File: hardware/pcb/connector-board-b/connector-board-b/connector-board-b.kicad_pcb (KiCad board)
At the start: 2 copper layers, 21.3 x 50.5 mm, 4 parts, among them J1 DE9_Pins, J3 Conn_01x02, J4 Conn_01x02, J5 8-215570-0

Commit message: Updated Connectorboard B to rev. 1.1
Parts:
- removed J3: Conn_01x02, TerminalBlock:TerminalBlock_MaiXu_MX126-5.0-02P_1x02_P5.00mm
- removed J4: Conn_01x02, Connector_JST:JST_EH_B2B-EH-A_1x02_P2.50mm_Vertical
- added C1: 10u 50V, Capacitor_SMD:C_1210_3225Metric, F.Cu at (159.1, 49.8)
- added C10: 100n, Capacitor_SMD:C_0805_2012Metric, F.Cu at (148.4, 51.1)
- added C11: 10u, Capacitor_SMD:C_1206_3216Metric, F.Cu at (145.3, 46.9)
- added C12: 100n, Capacitor_SMD:C_0805_2012Metric, F.Cu at (150.9, 64.3)
- added C13: 1n DNP, Capacitor_SMD:C_0805_2012Metric, F.Cu at (142.3, 79.1)
- added C14: 1u, Capacitor_SMD:C_0805_2012Metric, F.Cu at (147.1, 56.2)
- added C15: 1u, Capacitor_SMD:C_0805_2012Metric, F.Cu at (150.0, 55.9)
- added C2: 10u 50V, Capacitor_SMD:C_1210_3225Metric, F.Cu at (163.3, 49.8)
- added C3: 100n, Capacitor_SMD:C_0805_2012Metric, F.Cu at (154.4, 74.7)
- added C4: 1u, Capacitor_SMD:C_0805_2012Metric, F.Cu at (153.4, 76.7)
- added C5: 100n, Capacitor_SMD:C_0805_2012Metric, F.Cu at (145.9, 74.2)
- added C6: 1u, Capacitor_SMD:C_0805_2012Metric, F.Cu at (154.2, 79.2)
- added C7: 1u, Capacitor_SMD:C_0805_2012Metric, F.Cu at (152.1, 86.4)
- added C8: 10u, Capacitor_SMD:C_1206_3216Metric, F.Cu at (148.8, 48.0)
- added C9: 10u, Capacitor_SMD:C_1206_3216Metric, F.Cu at (153.4, 48.0)
- added D1: BAT42W, Diode_SMD:D_SOD-123, F.Cu at (150.2, 74.2)
- added D2: CHG (RED), LED_SMD:LED_0805_2012Metric, F.Cu at (166.2, 79.0)
- added D3: DONE (GRN), LED_SMD:LED_0805_2012Metric, F.Cu at (166.2, 81.3)
- added F1: PTC 3A (SMD1812P300TF/16), Fuse:Fuse_1812_4532Metric, F.Cu at (144.4, 42.4)
- added F2: PTC 0.35A (SMD1206P035TF/30), Fuse:Fuse_1206_3216Metric, F.Cu at (148.0, 89.5)
- added J2: PANEL_18V, TerminalBlock:TerminalBlock_MaiXu_MX126-5.0-02P_1x02_P5.00mm, F.Cu at (163.8, 90.9)
- added J6: NTC_103AT, Connector_JST:JST_PH_B2B-PH-K_1x02_P2.00mm_Vertical, F.Cu at (143.5, 88.1)
- added J7: BATTERY, Connector_JST:JST_EH_B2B-EH-A_1x02_P2.50mm_Vertical, F.Cu at (143.8, 36.8)
- added L1: 10u, Inductor_SMD:L_Vishay_IHLP-4040, F.Cu at (146.8, 58.4)
- added Q1: Si4840BDY, Package_SO:SOIC-8_3.9x4.9mm_P1.27mm, F.Cu at (144.0, 69.1)
- added Q2: Si4840BDY, Package_SO:SOIC-8_3.9x4.9mm_P1.27mm, F.Cu at (149.6, 69.1)
- added R1: 499k 1%, Resistor_SMD:R_0805_2012Metric, F.Cu at (145.0, 77.7)
- added R11: 2R2 DNP, Resistor_SMD:R_0805_2012Metric, F.Cu at (142.5, 75.3)
- added R2: 36k 1%, Resistor_SMD:R_0805_2012Metric, F.Cu at (145.0, 81.3)
- added R3: 499k 1%, Resistor_SMD:R_0805_2012Metric, F.Cu at (151.5, 81.8)
- added R4: 499k 1%, Resistor_SMD:R_0805_2012Metric, F.Cu at (155.1, 81.8)
- added R5: 5k23 1%, Resistor_SMD:R_0805_2012Metric, F.Cu at (152.4, 84.3)
- added R6: 30k1 1%, Resistor_SMD:R_0805_2012Metric, F.Cu at (148.9, 84.3)
- added R7: 2k, Resistor_SMD:R_0805_2012Metric, F.Cu at (162.8, 79.0)
- added R8: 2k, Resistor_SMD:R_0805_2012Metric, F.Cu at (162.8, 81.3)
- added RS1: 0R02 1%, Resistor_SMD:R_1206_3216Metric, F.Cu at (143.8, 50.8)
- added RS2: 0R10 1%, Resistor_SMD:R_1206_3216Metric, F.Cu at (157.0, 91.4)
- added RS3: 0R02 1%, Resistor_SMD:R_1206_3216Metric, F.Cu at (142.7, 47.0)
- added RS4: 0R05 1%, Resistor_SMD:R_1206_3216Metric, F.Cu at (152.9, 51.1)
- added SW1: PWR_KILL, connector-board-b:SW_Toggle_CAX_MTS202C3D1_RightAngle, F.Cu at (153.4, 39.2)
- added U1: BQ24650RVA, solar_charger:Texas_RVA0016A_VQFN-16-1EP_3.5x3.5mm_P0.5mm_EP2.1x2.1mm, F.Cu at (148.8, 78.2)
- added U2: INA3221, Package_DFN_QFN:Texas_RGV0016A_VQFN-16-1EP_4x4mm_P0.65mm_EP2.1x2.1mm, F.Cu at (147.1, 63.5)
- added U3: MCP1700-3.3, Package_TO_SOT_SMD:SOT-23, F.Cu at (150.1, 59.4)
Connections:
- net Net-(J1-Pad3) renamed LORA_nRESET
- net Net-(J1-Pad4) renamed LORA_SWDCLK
- net Net-(J1-Pad5) renamed LORA_SWDIO
- net Net-(J1-Pad6) renamed LORA_PWR_KILL
- net Net-(J1-Pad8) renamed WALTER_TX
- net Net-(J1-Pad9) renamed WALTER_RX
- J1 pad 2: VCC -> VBAT_OUT
- J1 pad 7: Net-(J1-Pad7) -> unconnected-(J1-Pad7)
- J5 pad 10: unconnected-(J5-Pad10) -> I2C_SCL
- J5 pad 2: VCC -> VBAT_RAW
- J5 pad 7: Net-(J1-Pad7) -> I2C_SDA
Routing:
- net VCC: track 66.8 -> 0.00 mm
- net GND: track 54.6 -> 0.00 mm
- net LORA_SWDIO: track 41.2 -> 0.00 mm, vias 2 -> 0
- net WALTER_RX: track 40.1 -> 0.00 mm
- net LORA_nRESET: track 37.7 -> 0.00 mm, vias 2 -> 0
- net LORA_SWDCLK: track 36.9 -> 0.00 mm, vias 2 -> 0
- net WALTER_TX: track 34.2 -> 0.00 mm
- net Net-(J1-Pad7): track 33.6 -> 0.00 mm
- net LORA_PWR_KILL: track 27.3 -> 0.00 mm
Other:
- board size 21.3 x 50.5 mm -> 27.4 x 70.6 mm
- board text added: "Connector board B v1.1 TwinOak Standard Repeater"
- board text removed: "Connector board B v1.0 TwinOak Standard Repeater"

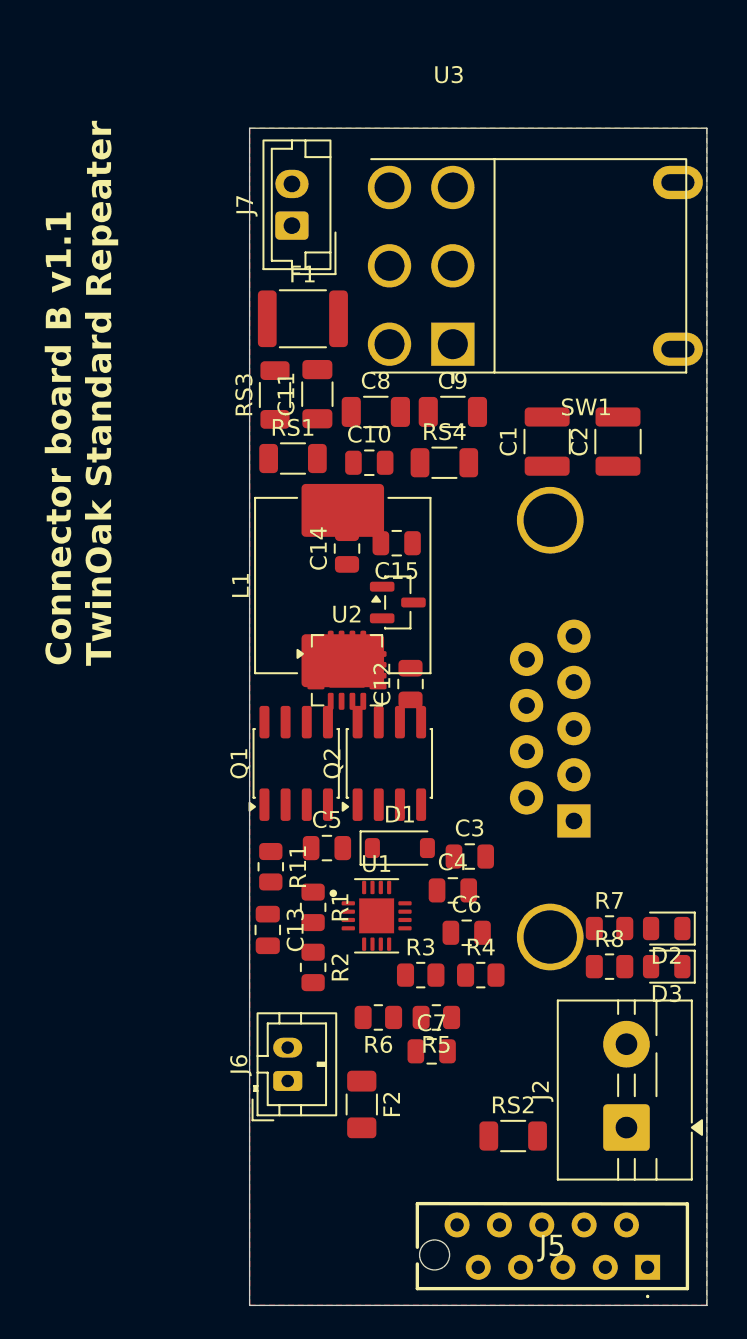
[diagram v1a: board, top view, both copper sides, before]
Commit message: Routing of connector b board
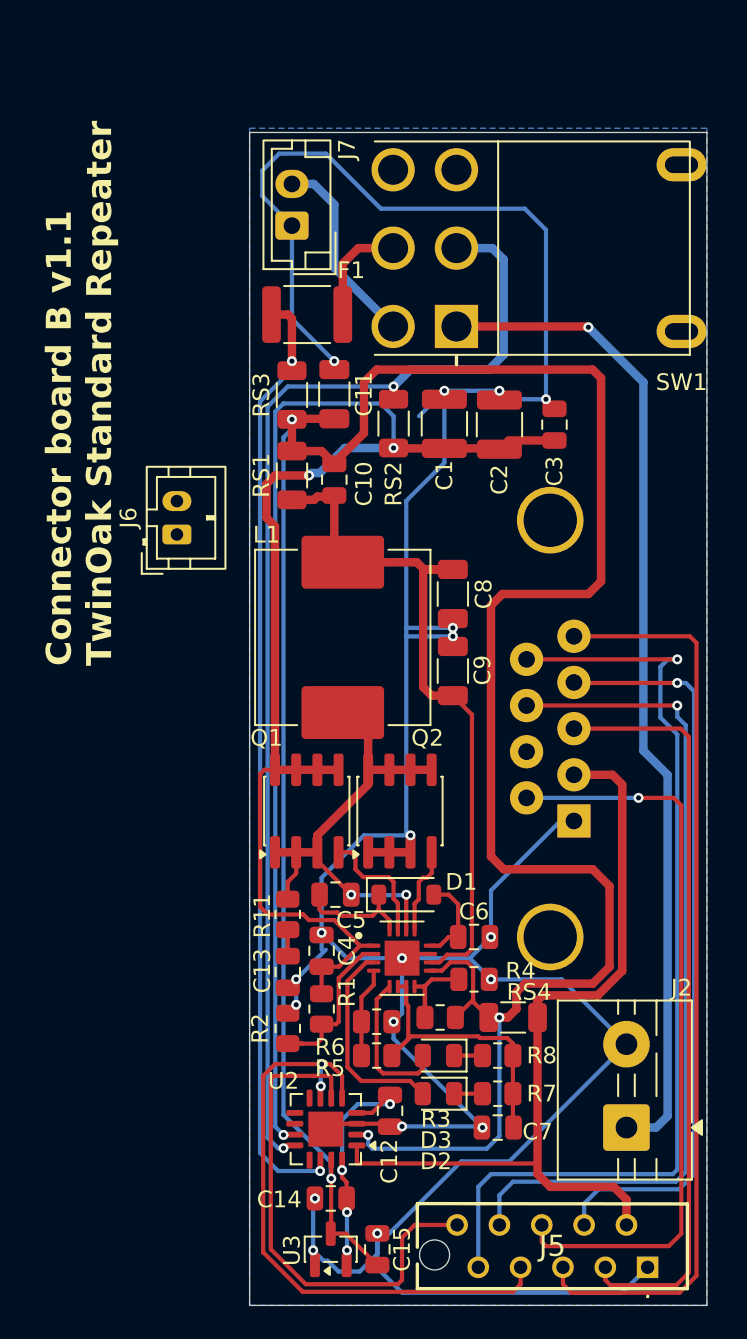
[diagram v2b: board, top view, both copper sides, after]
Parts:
- removed F2: PTC 0.35A (SMD1206P035TF/30), Fuse:Fuse_1206_3216Metric
- J5: footprint TwinOak platform footprints:82155700 -> TwinOak:82155700
- SW1: footprint connector-board-b:SW_Toggle_CAX_MTS202C3D1_RightAngle -> TwinOak:SW_Toggle_CAX_MTS202C3D1_RightAngle
- U1: footprint solar_charger:Texas_RVA0016A_VQFN-16-1EP_3.5x3.5mm_P0.5mm_EP2.1x2.1mm -> TwinOak:Texas_RVA0016A_VQFN-16-1EP_3.5x3.5mm_P0.5mm_EP2.1x2.1mm
- moved RS2 43.3 mm to (149.9, 48.7), turned to -90 degrees
- moved C15 42.4 mm to (148.9, 98.2), turned to 90 degrees
- moved U3 39.0 mm to (146.1, 98.2), turned to 90 degrees
- moved C14 39.0 mm to (146.1, 95.2), turned to 180 degrees
- moved RS4 33.5 mm to (157.0, 84.3)
- moved J6 33.4 mm to (136.9, 55.4)
- moved U2 27.6 mm to (145.8, 91.0), turned to 180 degrees
- moved C3 26.4 mm to (159.5, 48.8), turned to 90 degrees
- moved C12 25.6 mm to (149.6, 89.9), turned to -90 degrees
- moved D2 16.9 mm to (152.6, 88.9)
- moved C9 15.5 mm to (153.4, 63.5), turned to 90 degrees
- moved D3 14.7 mm to (152.6, 86.6)
- moved R7 12.0 mm to (156.1, 88.9), turned to 180 degrees
- moved C8 11.9 mm to (153.4, 58.9), turned to -90 degrees
- moved C4 8.67 mm to (145.5, 80.3), turned to 90 degrees
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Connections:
- net 3V3T renamed Net-(U2-VPU)
- net BAT_SW renamed BAT+
- C10 pad 2: VBAT -> VCC
- C11 pad 1: VBAT -> VCC
- C15 pad 1: VBAT -> VCC
- F1 pad 1: VBAT_SNS -> VBAT
- J1 pad 2: VBAT_OUT -> VLOAD+
- J5 pad 2: VBAT_RAW -> VLOAD+
- R3 pad 1: VBAT -> VCC
- R7 pad 2: Net-(D2-A) -> Net-(D2-K)
- R8 pad 2: Net-(D3-A) -> Net-(D3-K)
- RS1 pad 2: VBAT -> VCC
- RS3 pad 1: VBAT -> VCC
- RS3 pad 2: VBAT_SNS -> VBAT
- RS4 pad 1: VBAT -> VCC
- RS4 pad 2: VBAT_OUT -> VLOAD+
- U1 pad 3: Net-(D2-K) -> Net-(D2-A)
- U1 pad 5: Net-(D3-K) -> Net-(D3-A)
- U1 pad 9: VBAT -> VCC
- U2 pad 1: VBAT_OUT -> VLOAD+
- U2 pad 14: VBAT_SNS -> VBAT
- U2 pad 15: VBAT -> VCC
- U2 pad 2: VBAT -> VCC
- U3 pad 3: VBAT -> VCC
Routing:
- net GND: track 0.00 -> 213.0 mm, vias 0 -> 19
- net VCC: track 0.00 -> 163.3 mm, vias 0 -> 4
- net VIN: track 0.00 -> 114.1 mm, vias 0 -> 3
- net PANEL+: track 0.00 -> 70.9 mm, vias 0 -> 2
- net PANEL_RAW: track 0.00 -> 60.0 mm, vias 0 -> 1
- net WALTER_RX: track 0.00 -> 58.0 mm, vias 0 -> 1
- net VBAT: track 0.00 -> 58.0 mm, vias 0 -> 2
- net LORA_SWDIO: track 0.00 -> 55.1 mm
- net VLOAD+: track 0.00 -> 51.6 mm
- net WALTER_TX: track 0.00 -> 50.8 mm, vias 0 -> 1
- net LORA_nRESET: track 0.00 -> 45.5 mm
- net LORA_SWDCLK: track 0.00 -> 45.0 mm, vias 0 -> 1
- net LORA_PWR_KILL: track 0.00 -> 45.0 mm, vias 0 -> 1
- net Net-(U1-SRP): track 0.00 -> 43.0 mm
- net I2C_SDA: track 0.00 -> 36.9 mm, vias 0 -> 2
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- added copper zone on B.Cu, net GND
- removed copper zone on F.Cu, net GND
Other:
- board size 27.4 x 70.6 mm -> 27.4 x 70.4 mm

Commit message: Cleanup. Added feedback prevention circuits to Walter adapter
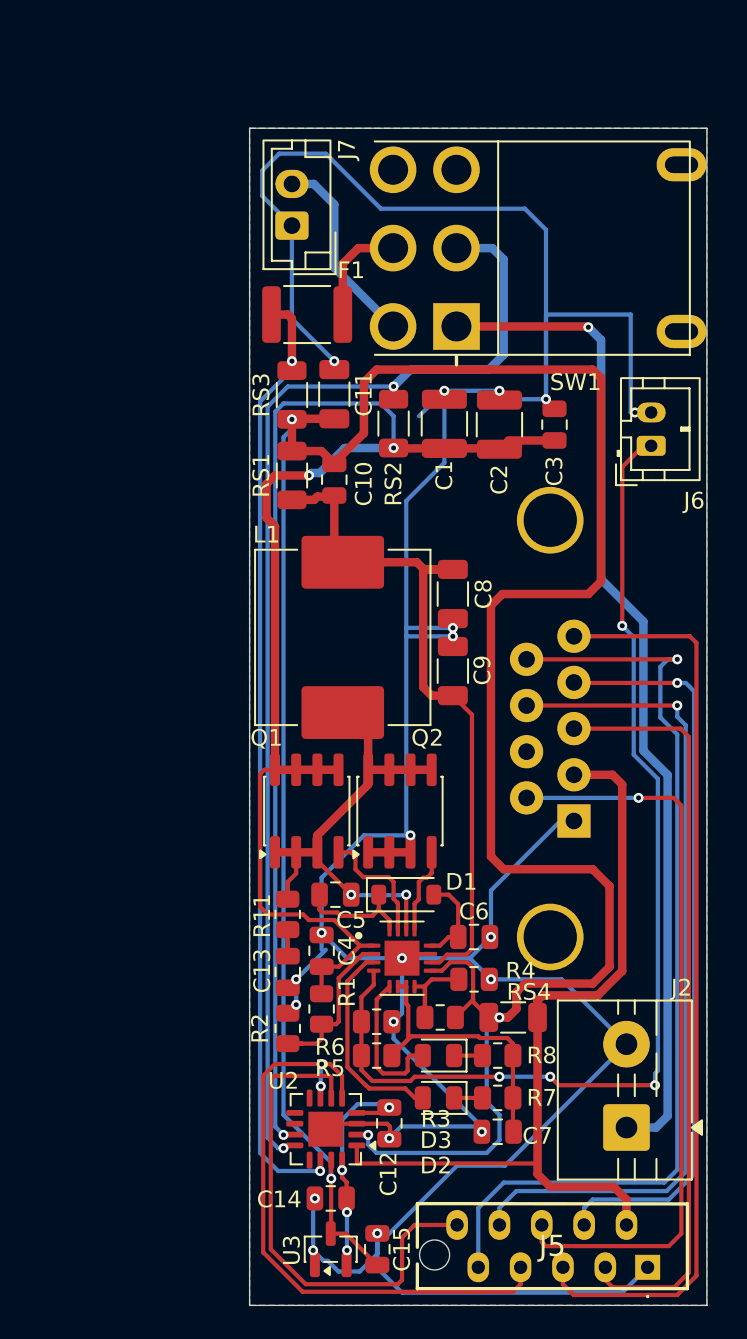
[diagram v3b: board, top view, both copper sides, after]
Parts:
- moved J6 28.9 mm to (165.3, 50.0)
- moved C12 0.75 mm to (149.6, 90.7)
- moved C7 0.25 mm to (156.1, 91.2)
- moved D2 0.25 mm to (152.6, 89.2)
- moved R7 0.25 mm to (156.1, 89.2)
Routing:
- net Net-(J6-Pin_1): track 5.40 -> 64.3 mm, vias 0 -> 4
- net GND: track 213.0 -> 231.1 mm, vias 19 -> 20
- net VCC: track 163.3 -> 164.3 mm
- net WALTER_RX: track 58.0 -> 57.3 mm
- added copper zone on F.Cu, net GND
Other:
- board size 27.4 x 70.4 mm -> 27.4 x 70.6 mm

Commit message: Minor connector b updates
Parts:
- moved D2 0.10 mm to (152.7, 89.2), turned to 0 degrees
- moved D3 0.10 mm to (152.7, 86.6), turned to 0 degrees
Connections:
- R7 pad 2: Net-(D2-K) -> Net-(D2-A)
- R8 pad 2: Net-(D3-K) -> Net-(D3-A)
- U1 pad 3: Net-(D2-A) -> Net-(D2-K)
- U1 pad 5: Net-(D3-A) -> Net-(D3-K)
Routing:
- net Net-(D2-K): track 1.92 -> 13.0 mm
- net Net-(D2-A): track 12.6 -> 3.52 mm
- net Net-(D3-K): track 1.71 -> 9.06 mm
- net Net-(D3-A): track 8.96 -> 3.31 mm

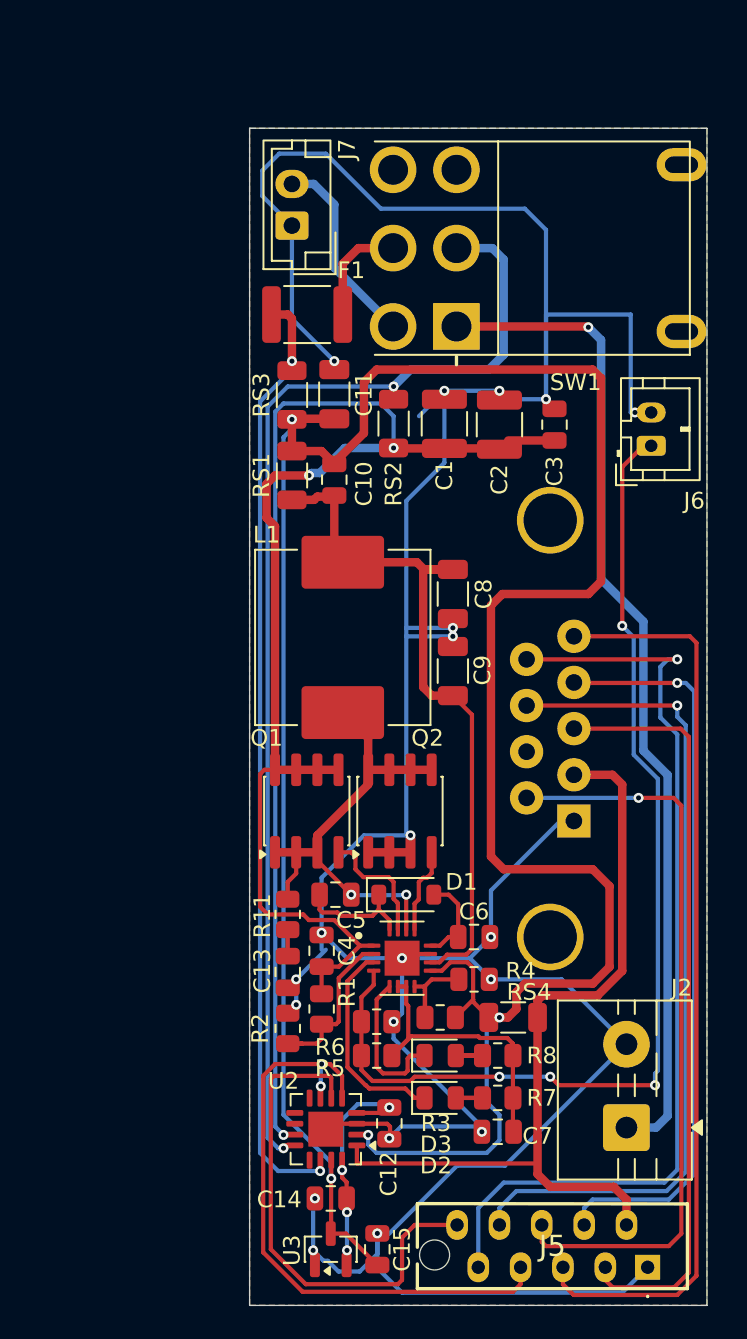
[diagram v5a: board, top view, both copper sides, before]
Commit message: Updates according to preflight
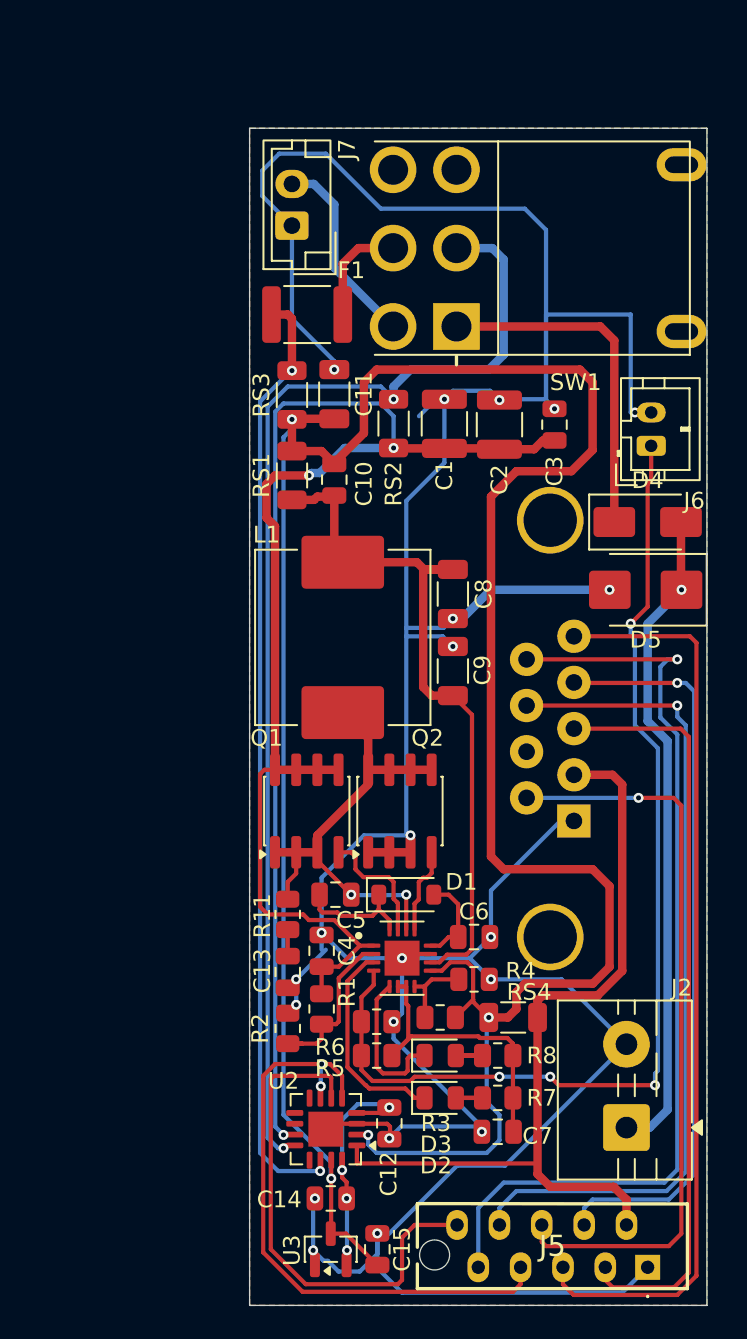
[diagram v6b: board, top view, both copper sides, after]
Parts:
- added D4: SS54, Diode_SMD:D_SMA, F.Cu at (165.1, 54.6)
- added D5: SMBJ26A, Diode_SMD:D_SMB, F.Cu at (165.0, 58.7)
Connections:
- J2 pad 1: PANEL_RAW -> Net-(D4-A)
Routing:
- net Net-(D4-A): track 0.00 -> 39.5 mm, vias 0 -> 1
- net PANEL_RAW: track 60.0 -> 20.7 mm, vias 1 -> 0
- net GND: track 231.1 -> 240.5 mm, vias 20 -> 21
- net VCC: track 164.3 -> 162.1 mm
- net VBAT: track 58.0 -> 56.9 mm
